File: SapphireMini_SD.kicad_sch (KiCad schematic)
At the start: 13 parts, among them J301 503182-1852, U301 MB85RS1MT

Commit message: Start of layout
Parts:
- C302, C303: footprint Capacitor_SMD:C_0603_1608Metric -> Capacitor_SMD:C_0402_1005Metric
- R303, R304, R308, R309: MPN (none) -> CRCW060347R0FKEAC
- R310: MPN CRCW060347K5FKEAC -> RMCF0603ZT0R00
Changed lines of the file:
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@@
       (effects (font (size 1.27 1.27)) (justify left))
     )
-    (property "Footprint" "Capacitor_SMD:C_0603_1608Metric" (id 2) (at 154.94 106.68 0)
+    (property "Footprint" "Capacitor_SMD:C_0402_1005Metric" (id 2) (at 154.94 106.68 0)
       (effects (font (size 1.27 1.27)) hide)
     )
@@
       (effects (font (size 1.27 1.27)) hide)
     )
+    (property "Description" "47 Ohms ±1% 0.1W, 1/10W Chip Resistor 0603" (id 4) (at 207.01 76.2 0)
+      (effects (font (size 1.27 1.27)) hide)
+    )
+    (property "MPN" "CRCW060347R0FKEAC" (id 5) (at 207.01 76.2 0)
+      (effects (font (size 1.27 1.27)) hide)
+    )
     (pin "1")
     (pin "2")
@@
       (effects (font (size 1.27 1.27)) hide)
     )
+    (property "Description" "47 Ohms ±1% 0.1W, 1/10W Chip Resistor 0603" (id 4) (at 90.17 97.79 0)
+      (effects (font (size 1.27 1.27)) hide)
+    )
+    (property "MPN" "CRCW060347R0FKEAC" (id 5) (at 90.17 97.79 0)
+      (effects (font (size 1.27 1.27)) hide)
+    )
     (pin "1")
     (pin "2")
@@
       (effects (font (size 1.27 1.27)) hide)
     )
+    (property "Description" "47 Ohms ±1% 0.1W, 1/10W Chip Resistor 0603" (id 4) (at 210.82 93.98 0)
+      (effects (font (size 1.27 1.27)) hide)
+    )
+    (property "MPN" "CRCW060347R0FKEAC" (id 5) (at 210.82 93.98 0)
+      (effects (font (size 1.27 1.27)) hide)
+    )
     (pin "1")
     (pin "2")
@@
       (effects (font (size 1.27 1.27)) (justify left))
     )
-    (property "Footprint" "Capacitor_SMD:C_0603_1608Metric" (id 2) (at 33.02 90.17 0)
+    (property "Footprint" "Capacitor_SMD:C_0402_1005Metric" (id 2) (at 33.02 90.17 0)
       (effects (font (size 1.27 1.27)) hide)
     )
@@
       (effects (font (size 1.27 1.27)) hide)
     )
+    (property "Description" "47 Ohms ±1% 0.1W, 1/10W Chip Resistor 0603" (id 4) (at 90.17 95.25 0)
+      (effects (font (size 1.27 1.27)) hide)
+    )
+    (property "MPN" "CRCW060347R0FKEAC" (id 5) (at 90.17 95.25 0)
+      (effects (font (size 1.27 1.27)) hide)
+    )
     (pin "1")
     (pin "2")
@@
       (effects (font (size 1.27 1.27)) hide)
     )
-    (property "MPN" "CRCW060347K5FKEAC" (id 6) (at 227.33 106.68 0)
+    (property "MPN" "RMCF0603ZT0R00" (id 6) (at 227.33 106.68 0)
       (effects (font (size 1.27 1.27)) hide)
     )
@@
       (effects (font (size 1.27 1.27)) hide)
     )
-    (property "Description" "47.5 kOhms ±1% 0.1W, 1/10W Chip Resistor 0603" (id 13) (at 227.33 106.68 0)
-      (effects (font (size 1.27 1.27)) hide)
-    )
+    (property "Description" "0 Ohms Jumper 0.1W, 1/10W Chip Resistor 0603 (1608 Metric) Automotive AEC-Q200 Thick Film" (id 13) (at 227.33 106.68 0)
+      (effects (font (size 1.27 1.27)) hide)
+    )

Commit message: updated new layout - no routing
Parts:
- J301: symbol 503182-1852:503182-1852 -> sapphireMini:503182-1852
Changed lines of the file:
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@@
     (pin "1")
   )
-  (symbol (lib_id "503182-1852:503182-1852") (at 236.22 99.06 0) (unit 1)
+  (symbol (lib_id "sapphireMini:503182-1852") (at 236.22 99.06 0) (unit 1)
     (in_bom yes) (on_board yes)
     (property "Reference" "J301" (id 0) (at 249.682 98.2253 0)

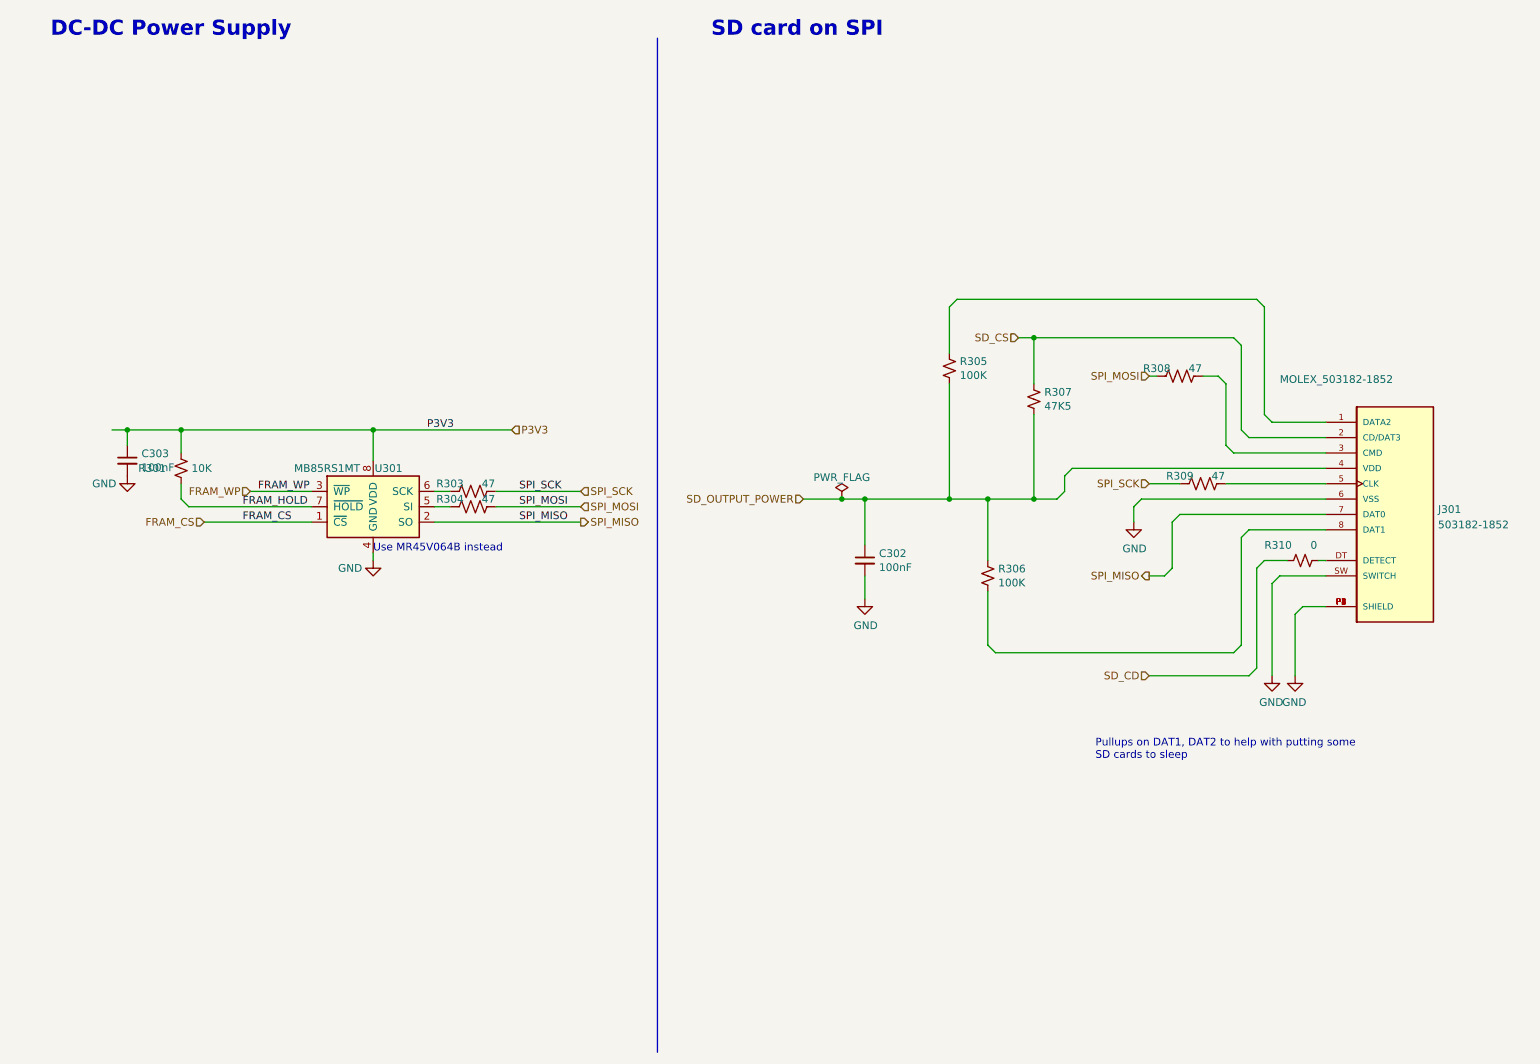
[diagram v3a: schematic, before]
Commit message: 6 Layer Routing
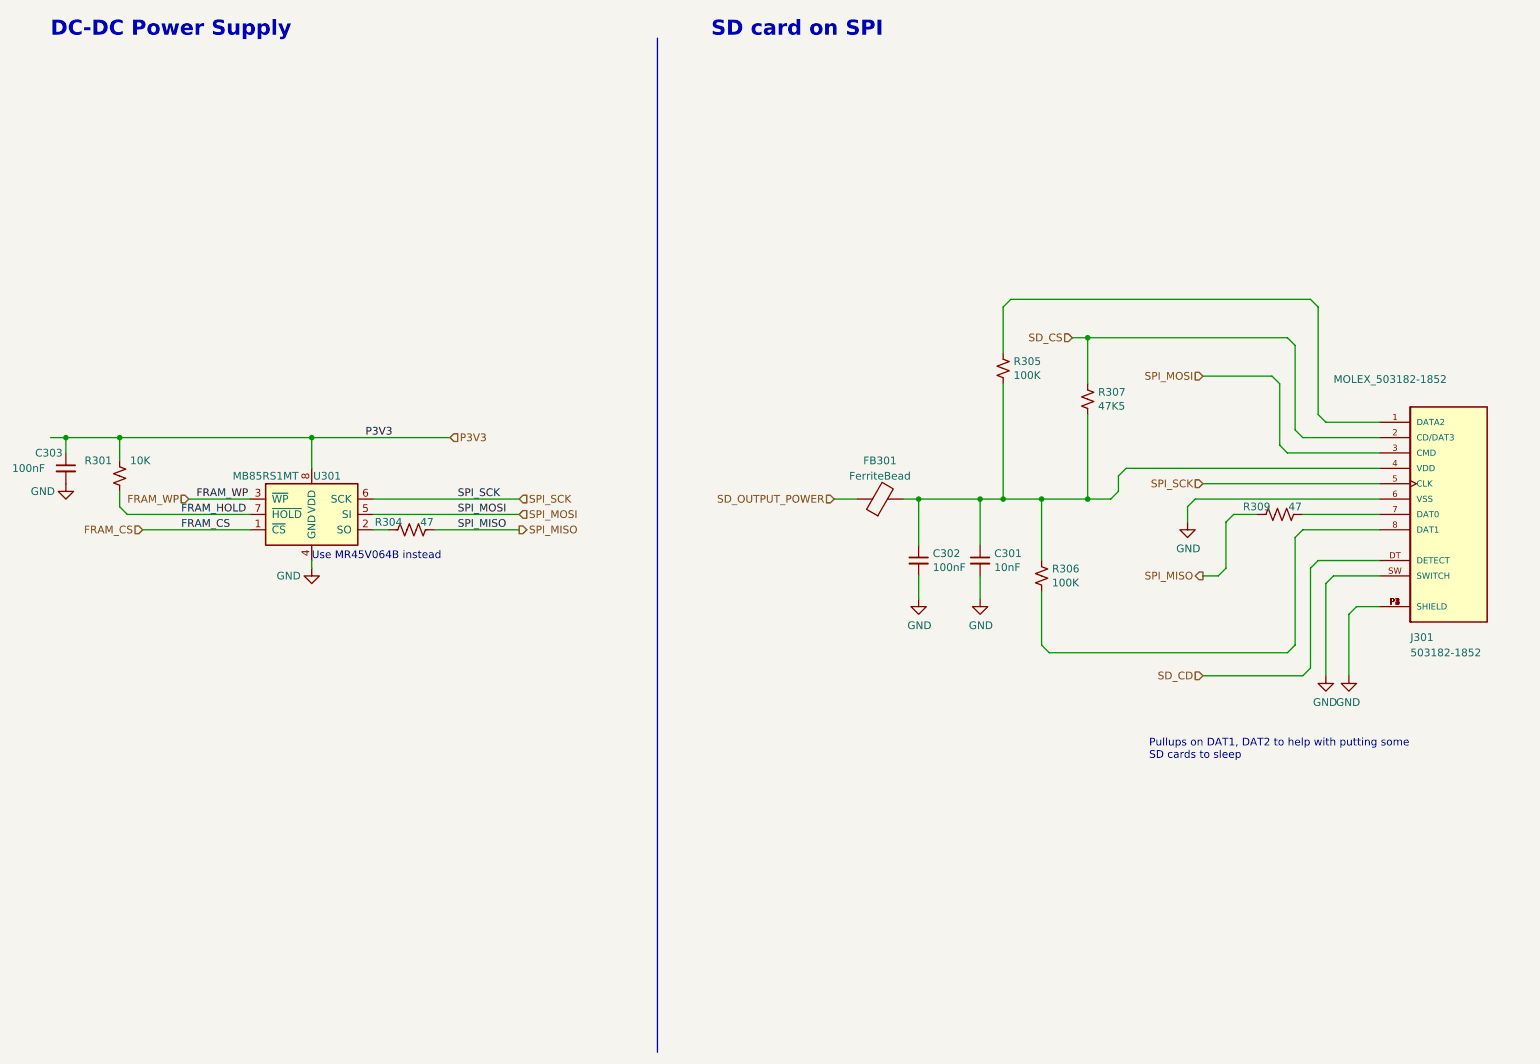
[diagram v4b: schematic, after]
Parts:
- removed R303, R308: 47, Resistor_SMD:R_0603_1608Metric, symbol Device:R_US
- removed R310: 0, Resistor_SMD:R_0603_1608Metric, symbol Device:R_Small_US
- added C301: 10nF, Capacitor_SMD:C_0402_1005Metric, symbol Device:C_Small
- added FB301: FerriteBead, Inductor_SMD:L_0603_1608Metric, symbol Device:FerriteBead
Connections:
- net GND: now also C301.2
- net SD_CD: now also J301.DT (DETECT)
- net SD_OUTPUT_POWER: now also FB301.1; no longer C302.1, J301.4 (VDD), R305.2, R306.1, R307.1
- net SPI_MISO: now also R304.1, R309.2; no longer J301.7 (DAT0), U301.2 (SO)
- net SPI_MOSI: now also J301.3 (CMD), U301.5 (SI); no longer R304.1
- net SPI_SCK: now also J301.5 (CLK), U301.6 (SCK); no longer R309.2
- net at R304.2: now also U301.2 (SO); no longer U301.5 (SI)
- net at R309.1: now also J301.7 (DAT0); no longer J301.5 (CLK)
- new net: C301.1, C302.1, FB301.2, J301.4 (VDD), R305.2, R306.1, R307.1
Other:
- moved on the sheet: C302, C303, J301, R301, R304, R305, R306, R307, R309, U301

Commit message: Added optional RSCK footprint
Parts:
- C301: MPN (none) -> CL05B103KB5NNNC
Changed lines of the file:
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@@
       (effects (font (size 1.27 1.27)) hide)
     )
-    (property "MPN" "" (id 5) (at 173.99 106.68 0)
+    (property "MPN" "CL05B103KB5NNNC" (id 5) (at 173.99 106.68 0)
       (effects (font (size 1.27 1.27)) hide)
     )

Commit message: Fixing board problems
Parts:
- U301: value MB85RS1MT -> MB85RS2MTAPNF-G-BDERE1; MPN MR45V064BMAZAATL -> MB85RS2MTAPNF-G-BDERE1
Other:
- note added: "Alternative MR45V064B at lower price for less storage"
- note added: "MB85RS2MTAPNF-G-BDERE1 for U301 to provide 256K bytes storage"
- note removed: "Use MR45V064B instead"
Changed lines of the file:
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@@
     (effects (font (size 2.5 2.5) (thickness 0.5) bold) (justify left bottom))
   )
-  (text "Use MR45V064B instead" (at 63.5 106.68 0)
+  (text "Alternative MR45V064B\nat lower price for less\nstorage"
+    (at 36.83 85.09 0)
     (effects (font (size 1.27 1.27)) (justify left bottom))
   )
   (text "SD card on SPI" (at 129.54 20.32 0)
     (effects (font (size 2.5 2.5) (thickness 0.5) bold) (justify left bottom))
+  )
+  (text "MB85RS2MTAPNF-G-BDERE1 for U301 \nto provide 256K bytes storage"
+    (at 36.83 77.47 0)
+    (effects (font (size 1.27 1.27)) (justify left bottom))
   )
   (text "Pullups on DAT1, DAT2 to help with putting some\nSD cards to sleep"
@@
     (in_bom yes) (on_board yes)
     (property "Reference" "U301" (id 0) (at 66.04 92.71 0))
-    (property "Value" "MB85RS1MT" (id 1) (at 55.88 92.71 0))
+    (property "Value" "MB85RS2MTAPNF-G-BDERE1" (id 1) (at 55.88 90.17 0))
     (property "Footprint" "Package_SO:SOP-8_3.9x4.9mm_P1.27mm" (id 2) (at 54.61 100.33 0)
       (effects (font (size 1.27 1.27)) hide)
@@
       (effects (font (size 1.27 1.27)) hide)
     )
-    (property "MPN" "MR45V064BMAZAATL" (id 5) (at 63.5 99.06 0)
-      (effects (font (size 1.27 1.27)) hide)
-    )
+    (property "MPN" "MB85RS2MTAPNF-G-BDERE1" (id 5) (at 63.5 99.06 0)
+      (effects (font (size 1.27 1.27)) hide)
+    )

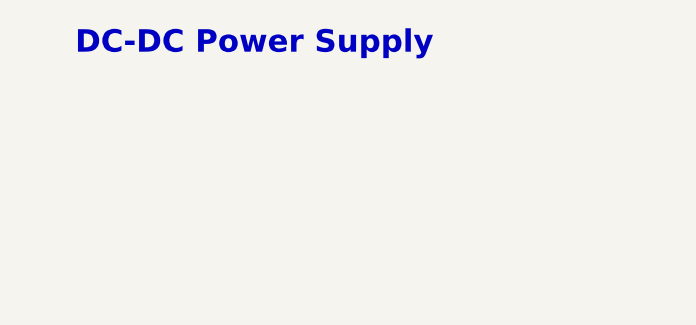
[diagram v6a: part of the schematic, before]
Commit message: Updated PCB comments
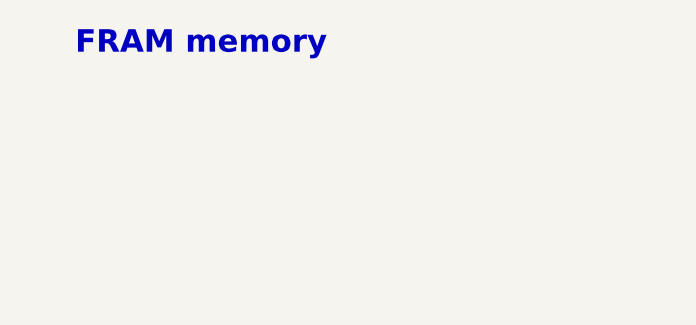
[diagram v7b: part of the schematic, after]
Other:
- note added: "FRAM memory"
- note removed: "DC-DC Power Supply"
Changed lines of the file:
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@@
     (stroke (width 0) (type default) (color 0 0 0 0))
   )
-  (text "DC-DC Power Supply" (at 20.32 20.32 0)
+  (text "FRAM memory" (at 20.32 20.32 0)
     (effects (font (size 2.5 2.5) (thickness 0.5) bold) (justify left bottom))
   )

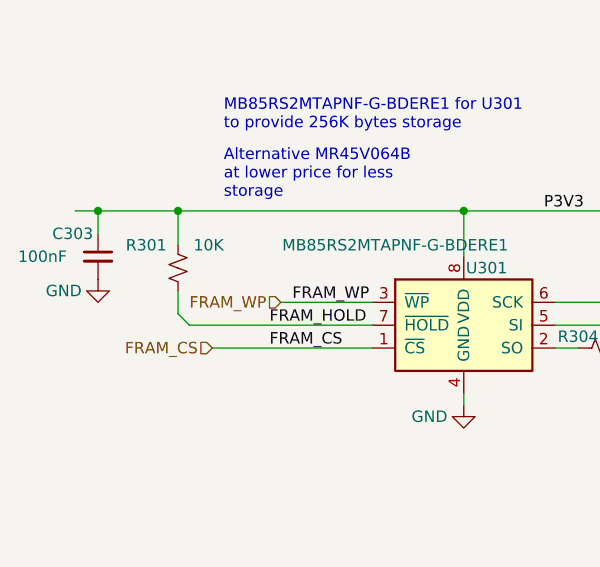
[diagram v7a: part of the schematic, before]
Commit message: Updated to fix noted problems
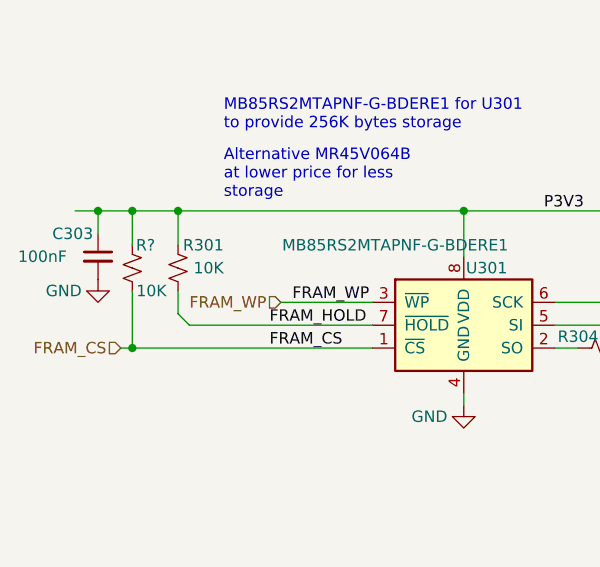
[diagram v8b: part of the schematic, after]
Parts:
- added R?: 10K, Resistor_SMD:R_0603_1608Metric, symbol Device:R_Small_US
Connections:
- net FRAM_CS: now also R?.1
- net P3V3: now also R?.2
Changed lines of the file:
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@@
     (comment 2 "Markup copy w/ errors!")
   )
+  (junction (at 26.67 86.36) (diameter 0) (color 0 0 0 0)
+  )
+  (junction (at 26.67 101.6) (diameter 0) (color 0 0 0 0)
+  )
   (junction (at 177.8 96.52) (diameter 0) (color 0 0 0 0)
   )
@@
     (stroke (width 0) (type default) (color 0 0 0 0))
   )
-  (wire (pts (xy 31.75 86.36) (xy 22.86 86.36))
+  (wire (pts (xy 26.67 101.6) (xy 53.34 101.6))
+    (stroke (width 0) (type default) (color 0 0 0 0))
+  )
+  (wire (pts (xy 31.75 86.36) (xy 26.67 86.36))
     (stroke (width 0) (type default) (color 0 0 0 0))
   )
@@
     (stroke (width 0) (type default) (color 0 0 0 0))
   )
-  (wire (pts (xy 35.56 101.6) (xy 53.34 101.6))
+  (wire (pts (xy 25.4 101.6) (xy 26.67 101.6))
     (stroke (width 0) (type default) (color 0 0 0 0))
   )
@@
     (stroke (width 0) (type default) (color 0 0 0 0))
   )
+  (wire (pts (xy 26.67 86.36) (xy 22.86 86.36))
+    (stroke (width 0) (type default) (color 0 0 0 0))
+  )
   (wire (pts (xy 196.85 95.25) (xy 195.58 96.52))
     (stroke (width 0) (type default) (color 0 0 0 0))
@@
     (stroke (width 0) (type default) (color 0 0 0 0))
   )
+  (wire (pts (xy 26.67 90.17) (xy 26.67 86.36))
+    (stroke (width 0) (type default) (color 0 0 0 0))
+  )
   (wire (pts (xy 231.14 83.82) (xy 240.03 83.82))
     (stroke (width 0) (type default) (color 0 0 0 0))
@@
   )
   (wire (pts (xy 228.6 63.5) (xy 179.07 63.5))
+    (stroke (width 0) (type default) (color 0 0 0 0))
+  )
+  (wire (pts (xy 26.67 95.25) (xy 26.67 101.6))
     (stroke (width 0) (type default) (color 0 0 0 0))
   )
@@
     (effects (font (size 1.27 1.27)) (justify left))
   )
-  (hierarchical_label "FRAM_CS" (shape input) (at 35.56 101.6 180)
+  (hierarchical_label "FRAM_CS" (shape input) (at 25.4 101.6 180)
     (effects (font (size 1.27 1.27)) (justify right))
   )
@@
   (symbol (lib_id "Device:R_Small_US") (at 31.75 92.71 180) (unit 1)
     (in_bom yes) (on_board yes)
-    (property "Reference" "R301" (id 0) (at 30.48 90.17 0)
-      (effects (font (size 1.27 1.27)) (justify left))
-    )
-    (property "Value" "10K" (id 1) (at 36.83 90.17 0)
+    (property "Reference" "R301" (id 0) (at 36.83 90.17 0)
+      (effects (font (size 1.27 1.27)) (justify left))
+    )
+    (property "Value" "10K" (id 1) (at 36.83 92.71 0)
       (effects (font (size 1.27 1.27)) (justify left))
     )
@@
       (effects (font (size 1.27 1.27)) hide)
     )
+    (pin "1")
+    (pin "2")
+  )
+  (symbol (lib_id "Device:R_Small_US") (at 26.67 92.71 180) (unit 1)
+    (in_bom yes) (on_board yes)
+    (property "Reference" "R?" (id 0) (at 29.21 90.17 0)
+      (effects (font (size 1.27 1.27)) (justify left))
+    )
+    (property "Value" "10K" (id 1) (at 30.48 95.25 0)
+      (effects (font (size 1.27 1.27)) (justify left))
+    )
+    (property "Footprint" "Resistor_SMD:R_0603_1608Metric" (id 2) (at 26.67 92.71 0)
+      (effects (font (size 1.27 1.27)) hide)
+    )
+    (property "Datasheet" "~" (id 3) (at 26.67 92.71 0)
+      (effects (font (size 1.27 1.27)) hide)
+    )
+    (property "DigiKey Price" "0.05" (id 4) (at 26.67 92.71 0)
+      (effects (font (size 1.27 1.27)) hide)
+    )
+    (property "Manufacturer" "Vishay" (id 5) (at 26.67 92.71 0)
+      (effects (font (size 1.27 1.27)) hide)
+    )
+    (property "MPN" "CRCW060347R0FKEAC" (id 6) (at 26.67 92.71 0)
+      (effects (font (size 1.27 1.27)) hide)
+    )
+    (property "Tolerance" "5%" (id 7) (at 26.67 92.71 0)
+      (effects (font (size 1.27 1.27)) hide)
+    )
+    (property "Populate" "1" (id 8) (at 26.67 92.71 0)
+      (effects (font (size 1.27 1.27)) hide)
+    )
+    (property "MacroFab_PN" "MF-RES-0603-2K" (id 9) (at 26.67 92.71 0)
+      (effects (font (size 1.27 1.27)) hide)
+    )
+    (property "Digi-Key_PN" "541-5440-1-ND" (id 10) (at 26.67 92.71 0)
+      (effects (font (size 1.27 1.27)) hide)
+    )
+    (property "Distributor" "Digikey" (id 11) (at 26.67 92.71 0)
+      (effects (font (size 1.27 1.27)) hide)
+    )
+    (property "DPN" "541-5440-1-ND" (id 12) (at 26.67 92.71 0)
+      (effects (font (size 1.27 1.27)) hide)
+    )
+    (property "Description" "47 Ohms ±1% 0.1W, 1/10W Chip Resistor 0603" (id 13) (at 26.67 92.71 0)
+      (effects (font (size 1.27 1.27)) hide)
+    )
